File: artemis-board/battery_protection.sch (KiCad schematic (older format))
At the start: 7 parts, among them J1 Battery connector, J7 DNP, U1 AP9101CK6-ADTRG1, U2 FS8205A

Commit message: swapped protection ic for the FS312F-G
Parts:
- U1: value AP9101CK6-ADTRG1 -> FS312F-G; LCSC C151339 -> C82736
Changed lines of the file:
@@
 P 5350 3350
 F 0 "U1" H 5350 2885 50  0000 C CNN
-F 1 "AP9101CK6-ADTRG1" H 5350 2976 50  0000 C CNN
+F 1 "FS312F-G" H 5350 2976 50  0000 C CNN
 F 2 "Package_TO_SOT_SMD:SOT-23-6_Handsoldering" H 5450 3800 50  0001 C CNN
-F 3 "https://www.diodes.com/assets/Datasheets/AP9101C.pdf" H 5350 3100 50  0001 C CNN
-F 4 "C151339" H 5350 3350 50  0001 C CNN "LCSC"
+F 3 "https://www.ic-fortune.com/upload/Download/FS312F-G-DS-12_EN.pdf" H 5350 3100 50  0001 C CNN
+F 4 "C82736" H 5350 3350 50  0001 C CNN "LCSC"
 	1    5350 3350
 	-1   0    0    1

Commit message: swapped and added some lcsc part numbers and DNP markers
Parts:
- J7: value DNP -> unprotected BAT in; DNP (none) -> DNP
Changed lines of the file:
@@
 P 6800 2550
 F 0 "J7" H 6700 2500 50  0000 C CNN
-F 1 "DNP" H 6900 2700 50  0000 C CNN
+F 1 "unprotected BAT in" H 6900 2700 50  0000 C CNN
 F 2 "Connector_JST:JST_PH_S2B-PH-K_1x02_P2.00mm_Horizontal" H 6800 2550 50  0001 C CNN
 F 3 "" H 6800 2550 50  0001 C CNN
 F 4 "" H 6800 2550 50  0001 C CNN "LCSC"
+F 5 "DNP" H 6800 2550 50  0001 C CNN "DNP"
 	1    6800 2550
 	1    0    0    -1

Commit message: added cap to Vbat rail for more stability
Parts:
- added C28: 22µF, Capacitor_SMD:C_0805_2012Metric, symbol Device:C
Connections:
- net GND: now also C28.2
- net VBAT: now also C28.1
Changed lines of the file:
@@
 Wire Wire Line
 	1100 1050 850  1050
+$Comp
+L Device:C C?
+U 1 1 60BF8CBC
+P 6950 4050
+AR Path="/5F63A0E9/60BF8CBC" Ref="C?"  Part="1"
+AR Path="/5F639CFE/60BF8CBC" Ref="C28"  Part="1"
+F 0 "C28" H 7065 4096 50  0000 L CNN
+F 1 "22µF" H 7065 4005 50  0000 L CNN
+F 2 "Capacitor_SMD:C_0805_2012Metric" H 6988 3900 50  0001 C CNN
+F 3 "~" H 6950 4050 50  0001 C CNN
+F 4 "C45783" H 6950 4050 50  0001 C CNN "LCSC"
+	1    6950 4050
+	1    0    0    -1
+$EndComp
+$Comp
+L power:GND #PWR0117
+U 1 1 60BF9399
+P 6950 4200
+F 0 "#PWR0117" H 6950 3950 50  0001 C CNN
+F 1 "GND" H 6955 4027 50  0000 C CNN
+F 2 "" H 6950 4200 50  0001 C CNN
+F 3 "" H 6950 4200 50  0001 C CNN
+	1    6950 4200
+	1    0    0    -1
+$EndComp
+Text Label 6950 3900 0    50   ~ 0
+BAT+
 $EndSCHEMATC

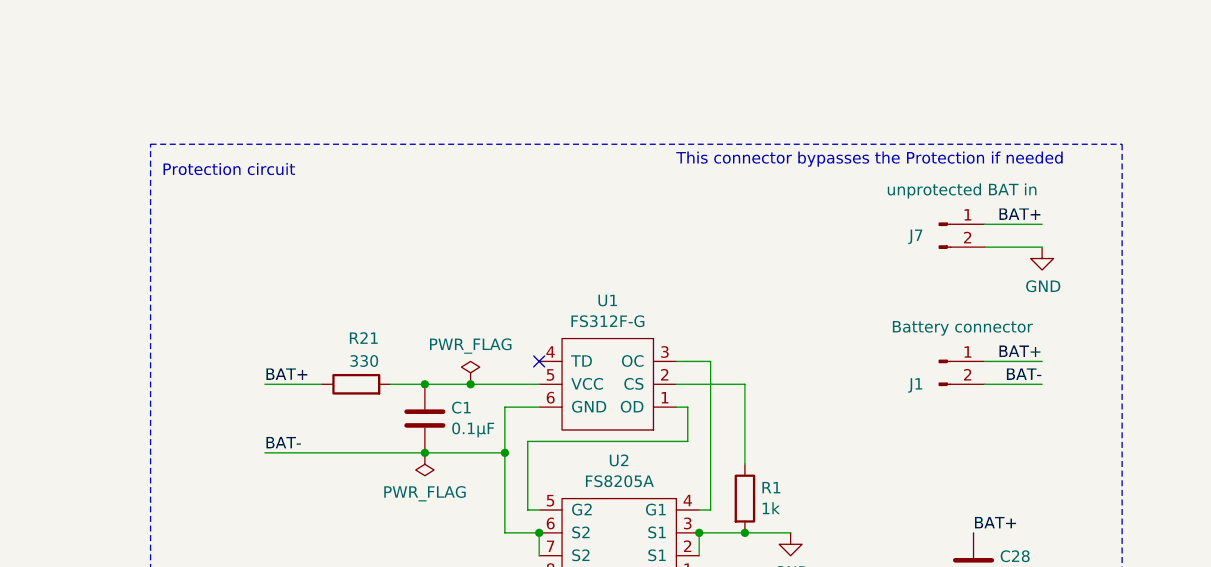
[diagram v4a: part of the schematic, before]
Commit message: removed unprotected connector, added jumper, moved cap to 3v3_mcu
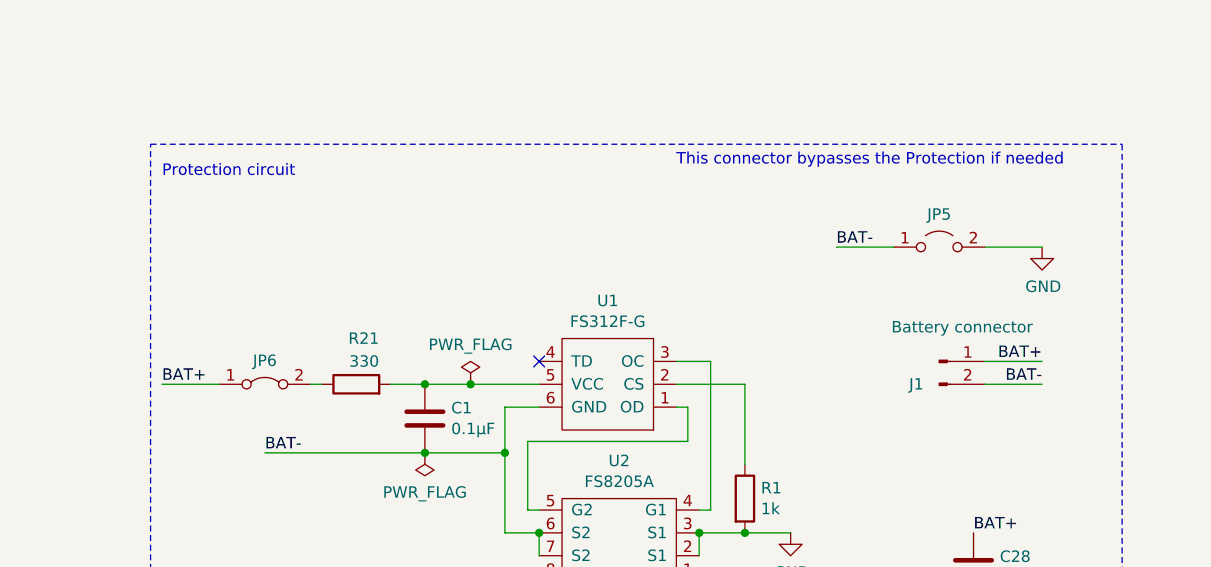
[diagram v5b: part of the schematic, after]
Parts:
- removed J7: unprotected BAT in, Connector_JST:JST_PH_S2B-PH-K_1x02_P2.00mm_Horizontal, symbol Connector:Conn_01x02_Male
- added JP5: Jumper_2_Open, Jumper:SolderJumper-2_P1.3mm_Open_Pad1.0x1.5mm, symbol Jumper:Jumper_2_Open
- added JP6: Jumper_2_Bridged, Jumper:SolderJumper-2_P1.3mm_Bridged_Pad1.0x1.5mm, symbol Jumper:Jumper_2_Bridged
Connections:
- net BAT-: now also JP5.1 (A)
- net GND: now also JP5.2 (B)
- net VBAT: now also JP6.1 (A); no longer R21.1
- new net: JP6.2 (B), R21.1
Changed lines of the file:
@@
 VBAT
 Wire Wire Line
-	3850 3250 4100 3250
+	3400 3250 3650 3250
 Text Notes 600  650  0    50   ~ 0
 Labels\n
@@
 Wire Wire Line
 	4750 3250 4550 3250
-$Comp
-L Connector:Conn_01x02_Male J7
-U 1 1 600973F8
-P 6800 2550
-F 0 "J7" H 6700 2500 50  0000 C CNN
-F 1 "unprotected BAT in" H 6900 2700 50  0000 C CNN
-F 2 "Connector_JST:JST_PH_S2B-PH-K_1x02_P2.00mm_Horizontal" H 6800 2550 50  0001 C CNN
-F 3 "" H 6800 2550 50  0001 C CNN
-F 4 "" H 6800 2550 50  0001 C CNN "LCSC"
-F 5 "DNP" H 6800 2550 50  0001 C CNN "DNP"
-	1    6800 2550
-	1    0    0    -1
-$EndComp
 Text Label 3850 3550 0    50   ~ 0
 BAT-
@@
 Text Label 7250 3150 2    50   ~ 0
 BAT+
-Text Label 3850 3250 0    50   ~ 0
+Text Label 3400 3250 0    50   ~ 0
 BAT+
-Text Label 7250 2550 2    50   ~ 0
-BAT+
-Wire Wire Line
-	7000 2550 7250 2550
 Text Label 1100 1050 2    50   ~ 0
 BAT+
@@
 Text Label 6950 3900 0    50   ~ 0
 BAT+
+$Comp
+L Jumper:Jumper_2_Open JP5
+U 1 1 60E838B6
+P 6800 2650
+F 0 "JP5" H 6800 2793 50  0000 C CNN
+F 1 "Jumper_2_Open" H 6800 2794 50  0001 C CNN
+F 2 "Jumper:SolderJumper-2_P1.3mm_Open_Pad1.0x1.5mm" H 6800 2650 50  0001 C CNN
+F 3 "~" H 6800 2650 50  0001 C CNN
+	1    6800 2650
+	1    0    0    -1
+$EndComp
+$Comp
+L Jumper:Jumper_2_Bridged JP6
+U 1 1 60E8440E
+P 3850 3250
+F 0 "JP6" H 3850 3353 50  0000 C CNN
+F 1 "Jumper_2_Bridged" H 3850 3354 50  0001 C CNN
+F 2 "Jumper:SolderJumper-2_P1.3mm_Bridged_Pad1.0x1.5mm" H 3850 3250 50  0001 C CNN
+F 3 "~" H 3850 3250 50  0001 C CNN
+	1    3850 3250
+	1    0    0    -1
+$EndComp
+Wire Wire Line
+	6600 2650 6350 2650
+Text Label 6350 2650 0    50   ~ 0
+BAT-
+Wire Wire Line
+	4050 3250 4100 3250
 $EndSCHEMATC

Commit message: added cap to 3v3 I2c, swapped some footprints to normal...
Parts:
- JP5, JP6: DNP (none) -> DNP
- U1: footprint Package_TO_SOT_SMD:SOT-23-6_Handsoldering -> Package_TO_SOT_SMD:SOT-23-6
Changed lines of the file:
@@
 F 0 "U1" H 5350 2885 50  0000 C CNN
 F 1 "FS312F-G" H 5350 2976 50  0000 C CNN
-F 2 "Package_TO_SOT_SMD:SOT-23-6_Handsoldering" H 5450 3800 50  0001 C CNN
+F 2 "Package_TO_SOT_SMD:SOT-23-6" H 5450 3800 50  0001 C CNN
 F 3 "https://www.ic-fortune.com/upload/Download/FS312F-G-DS-12_EN.pdf" H 5350 3100 50  0001 C CNN
 F 4 "C82736" H 5350 3350 50  0001 C CNN "LCSC"
@@
 F 2 "Jumper:SolderJumper-2_P1.3mm_Open_Pad1.0x1.5mm" H 6800 2650 50  0001 C CNN
 F 3 "~" H 6800 2650 50  0001 C CNN
+F 4 "DNP" H 6800 2650 50  0001 C CNN "DNP"
 	1    6800 2650
 	1    0    0    -1
@@
 F 2 "Jumper:SolderJumper-2_P1.3mm_Bridged_Pad1.0x1.5mm" H 3850 3250 50  0001 C CNN
 F 3 "~" H 3850 3250 50  0001 C CNN
+F 4 "DNP" H 3850 3250 50  0001 C CNN "DNP"
 	1    3850 3250
 	1    0    0    -1

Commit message: added comments, part numbers and extended marker
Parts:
- J1, U1, U2: Extended (none) -> Extended
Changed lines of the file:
@@
 F 3 "https://www.ic-fortune.com/upload/Download/FS312F-G-DS-12_EN.pdf" H 5350 3100 50  0001 C CNN
 F 4 "C82736" H 5350 3350 50  0001 C CNN "LCSC"
+F 5 "Extended" H 5350 3350 50  0001 C CNN "Extended"
 	1    5350 3350
 	-1   0    0    1
@@
 F 3 "https://www.ic-fortune.com/upload/Download/FS8205A-DS-12_EN.pdf" H 5400 4300 50  0001 C CNN
 F 4 "C16052" H 5400 4000 50  0001 C CNN "LCSC"
+F 5 "Extended" H 5400 4000 50  0001 C CNN "Extended"
 	1    5400 4000
 	-1   0    0    1
@@
 F 3 "https://datasheet.lcsc.com/szlcsc/1810261120_JST-Sales-America-S2B-PH-K-S-GW_C157932.pdf" H 6800 3150 50  0001 C CNN
 F 4 "C157932" H 6800 3150 50  0001 C CNN "LCSC"
+F 5 "Extended" H 6800 3150 50  0001 C CNN "Extended"
 	1    6800 3150
 	1    0    0    -1
